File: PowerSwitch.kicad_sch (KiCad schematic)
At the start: 5 parts

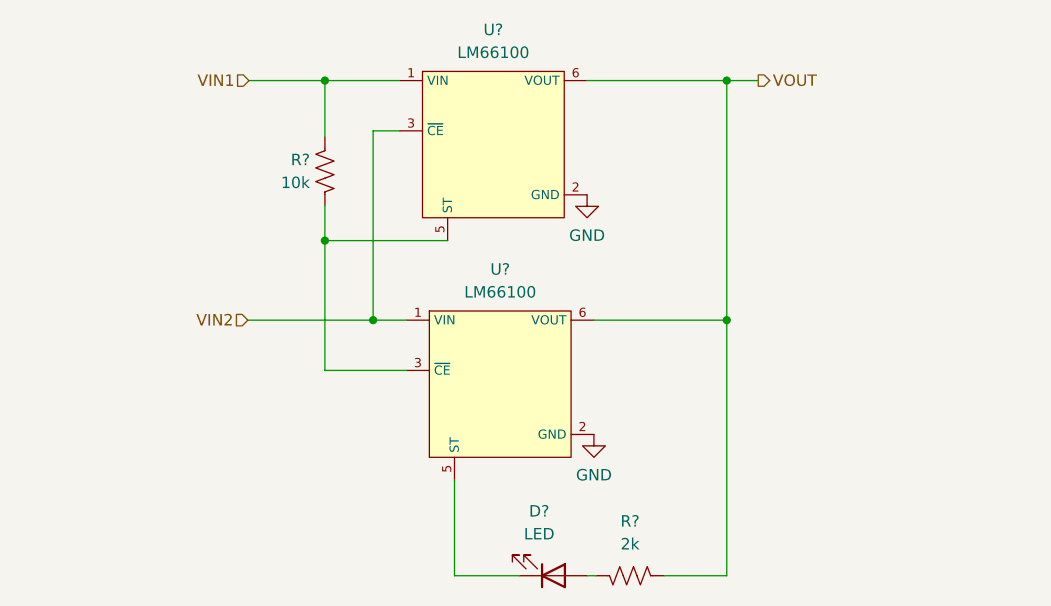
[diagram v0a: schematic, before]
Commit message: fixing sheet numbers and adding schematic PDF
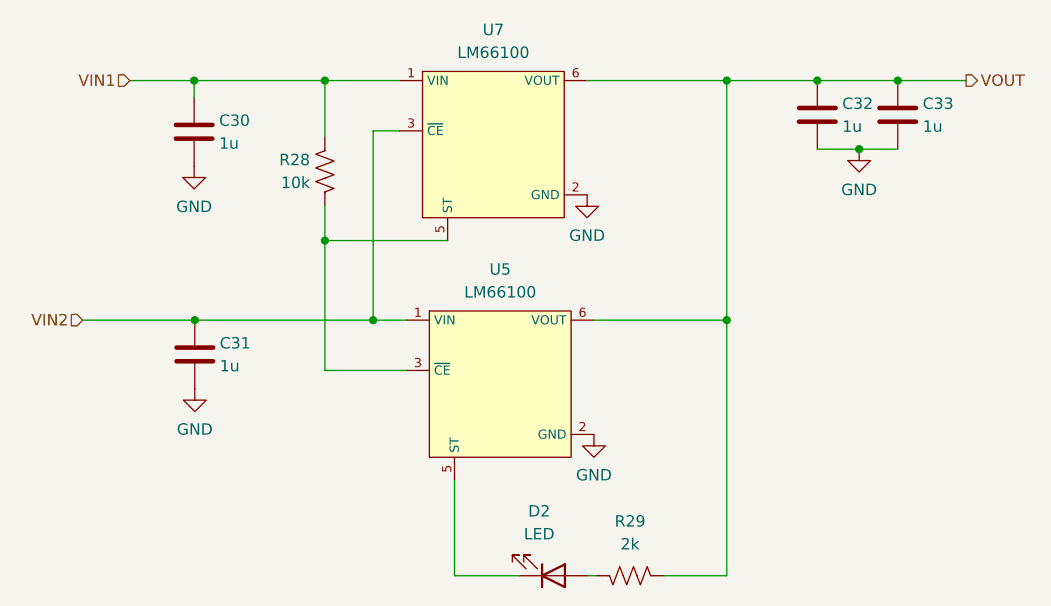
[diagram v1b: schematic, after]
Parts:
- added C30, C31, C32, C33: 1u, symbol Device:C
- gave numbers to parts that had none: 5
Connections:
- net GND: now also C30.2, C31.2, C32.2, C33.2
- net VIN1: now also C30.1
- net VIN2: now also C31.1
- net VOUT: now also C32.1, C33.1
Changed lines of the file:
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@@
   (junction (at 133.731 61.5188) (diameter 0) (color 0 0 0 0)
   )
+  (junction (at 119.2022 61.5188) (diameter 0) (color 0 0 0 0)
+  )
+  (junction (at 188.4426 61.5188) (diameter 0) (color 0 0 0 0)
+  )
   (junction (at 178.3842 88.138) (diameter 0) (color 0 0 0 0)
   )
@@
   (junction (at 133.731 79.2988) (diameter 0) (color 0 0 0 0)
   )
+  (junction (at 193.0908 69.1388) (diameter 0) (color 0 0 0 0)
+  )
+  (junction (at 119.2784 88.138) (diameter 0) (color 0 0 0 0)
+  )
+  (junction (at 197.3834 61.5188) (diameter 0) (color 0 0 0 0)
+  )
   (junction (at 178.3842 61.5188) (diameter 0) (color 0 0 0 0)
   )
+  (wire (pts (xy 119.2022 63.3984) (xy 119.2022 61.5188))
+    (stroke (width 0) (type default) (color 0 0 0 0))
+  )
   (wire (pts (xy 148.1328 116.5352) (xy 148.1328 105.918))
     (stroke (width 0) (type default) (color 0 0 0 0))
@@
     (stroke (width 0) (type default) (color 0 0 0 0))
   )
-  (wire (pts (xy 178.3842 61.5188) (xy 181.8894 61.5188))
+  (wire (pts (xy 178.3842 61.5188) (xy 188.4426 61.5188))
+    (stroke (width 0) (type default) (color 0 0 0 0))
+  )
+  (wire (pts (xy 119.2022 61.5188) (xy 133.731 61.5188))
     (stroke (width 0) (type default) (color 0 0 0 0))
   )
@@
     (stroke (width 0) (type default) (color 0 0 0 0))
   )
-  (wire (pts (xy 125.1712 88.138) (xy 139.0904 88.138))
+  (wire (pts (xy 106.8324 88.138) (xy 119.2784 88.138))
+    (stroke (width 0) (type default) (color 0 0 0 0))
+  )
+  (wire (pts (xy 119.2784 88.138) (xy 139.0904 88.138))
     (stroke (width 0) (type default) (color 0 0 0 0))
   )
@@
     (stroke (width 0) (type default) (color 0 0 0 0))
   )
+  (wire (pts (xy 188.4426 69.1388) (xy 193.0908 69.1388))
+    (stroke (width 0) (type default) (color 0 0 0 0))
+  )
   (wire (pts (xy 163.6268 88.138) (xy 178.3842 88.138))
     (stroke (width 0) (type default) (color 0 0 0 0))
   )
+  (wire (pts (xy 197.3834 61.5188) (xy 204.978 61.5188))
+    (stroke (width 0) (type default) (color 0 0 0 0))
+  )
   (wire (pts (xy 142.7988 93.726) (xy 133.731 93.726))
     (stroke (width 0) (type default) (color 0 0 0 0))
   )
-  (wire (pts (xy 125.2982 61.5188) (xy 133.731 61.5188))
+  (wire (pts (xy 188.4426 61.5188) (xy 197.3834 61.5188))
+    (stroke (width 0) (type default) (color 0 0 0 0))
+  )
+  (wire (pts (xy 112.0648 61.5188) (xy 119.2022 61.5188))
     (stroke (width 0) (type default) (color 0 0 0 0))
   )
@@
     (stroke (width 0) (type default) (color 0 0 0 0))
   )
-  (hierarchical_label "VIN1" (shape input) (at 125.2982 61.5188 180)
+  (wire (pts (xy 193.0908 69.1388) (xy 197.3834 69.1388))
+    (stroke (width 0) (type default) (color 0 0 0 0))
+  )
+  (hierarchical_label "VIN1" (shape input) (at 112.0648 61.5188 180)
     (effects (font (size 1.27 1.27)) (justify right))
   )
-  (hierarchical_label "VOUT" (shape output) (at 181.8894 61.5188 0)
+  (hierarchical_label "VOUT" (shape output) (at 204.978 61.5188 0)
     (effects (font (size 1.27 1.27)) (justify left))
   )
-  (hierarchical_label "VIN2" (shape input) (at 125.1712 88.138 180)
+  (hierarchical_label "VIN2" (shape input) (at 106.8324 88.138 180)
     (effects (font (size 1.27 1.27)) (justify right))
   )
   (symbol (lib_id "Device:R_US") (at 167.64 116.5352 270) (mirror x) (unit 1)
     (in_bom yes) (on_board yes) (fields_autoplaced)
-    (property "Reference" "R?" (id 0) (at 167.64 110.49 90))
+    (property "Reference" "R29" (id 0) (at 167.64 110.49 90))
     (property "Value" "2k" (id 1) (at 167.64 113.03 90))
     (property "Footprint" "" (id 2) (at 167.386 115.5192 90)
@@
     (pin "2")
   )
+  (symbol (lib_id "Device:C") (at 197.3834 65.3288 0) (unit 1)
+    (in_bom yes) (on_board yes)
+    (property "Reference" "C33" (id 0) (at 200.152 64.0842 0)
+      (effects (font (size 1.27 1.27)) (justify left))
+    )
+    (property "Value" "1u" (id 1) (at 200.152 66.6242 0)
+      (effects (font (size 1.27 1.27)) (justify left))
+    )
+    (property "Footprint" "" (id 2) (at 198.3486 69.1388 0)
+      (effects (font (size 1.27 1.27)) hide)
+    )
+    (property "Datasheet" "~" (id 3) (at 197.3834 65.3288 0)
+      (effects (font (size 1.27 1.27)) hide)
+    )
+    (pin "1")
+    (pin "2")
+  )
+  (symbol (lib_id "Device:C") (at 119.2022 67.2084 0) (unit 1)
+    (in_bom yes) (on_board yes)
+    (property "Reference" "C30" (id 0) (at 121.9708 65.9638 0)
+      (effects (font (size 1.27 1.27)) (justify left))
+    )
+    (property "Value" "1u" (id 1) (at 121.9708 68.5038 0)
+      (effects (font (size 1.27 1.27)) (justify left))
+    )
+    (property "Footprint" "" (id 2) (at 120.1674 71.0184 0)
+      (effects (font (size 1.27 1.27)) hide)
+    )
+    (property "Datasheet" "~" (id 3) (at 119.2022 67.2084 0)
+      (effects (font (size 1.27 1.27)) hide)
+    )
+    (pin "1")
+    (pin "2")
+  )
+  (symbol (lib_id "Device:C") (at 119.2784 91.948 0) (unit 1)
+    (in_bom yes) (on_board yes)
+    (property "Reference" "C31" (id 0) (at 122.047 90.7034 0)
+      (effects (font (size 1.27 1.27)) (justify left))
+    )
+    (property "Value" "1u" (id 1) (at 122.047 93.2434 0)
+      (effects (font (size 1.27 1.27)) (justify left))
+    )
+    (property "Footprint" "" (id 2) (at 120.2436 95.758 0)
+      (effects (font (size 1.27 1.27)) hide)
+    )
+    (property "Datasheet" "~" (id 3) (at 119.2784 91.948 0)
+      (effects (font (size 1.27 1.27)) hide)
+    )
+    (pin "1")
+    (pin "2")
+  )
+  (symbol (lib_id "power:GND") (at 119.2022 71.0184 0) (unit 1)
+    (in_bom yes) (on_board yes) (fields_autoplaced)
+    (property "Reference" "#PWR034" (id 0) (at 119.2022 77.3684 0)
+      (effects (font (size 1.27 1.27)) hide)
+    )
+    (property "Value" "GND" (id 1) (at 119.2022 75.5396 0))
+    (property "Footprint" "" (id 2) (at 119.2022 71.0184 0)
+      (effects (font (size 1.27 1.27)) hide)
+    )
+    (property "Datasheet" "" (id 3) (at 119.2022 71.0184 0)
+      (effects (font (size 1.27 1.27)) hide)
+    )
+    (pin "1")
+  )
+  (symbol (lib_id "power:GND") (at 193.0908 69.1388 0) (unit 1)
+    (in_bom yes) (on_board yes) (fields_autoplaced)
+    (property "Reference" "#PWR038" (id 0) (at 193.0908 75.4888 0)
+      (effects (font (size 1.27 1.27)) hide)
+    )
+    (property "Value" "GND" (id 1) (at 193.0908 73.66 0))
+    (property "Footprint" "" (id 2) (at 193.0908 69.1388 0)
+      (effects (font (size 1.27 1.27)) hide)
+    )
+    (property "Datasheet" "" (id 3) (at 193.0908 69.1388 0)
+      (effects (font (size 1.27 1.27)) hide)
+    )
+    (pin "1")
+  )
   (symbol (lib_id "Power_switch:LM66100") (at 153.4668 71.4248 0) (unit 1)
     (in_bom yes) (on_board yes) (fields_autoplaced)
-    (property "Reference" "U?" (id 0) (at 152.4508 55.88 0))
+    (property "Reference" "U7" (id 0) (at 152.4508 55.88 0))
     (property "Value" "LM66100" (id 1) (at 152.4508 58.42 0))
     (property "Footprint" "Package_TO_SOT_SMD:SOT-363_SC-70-6" (id 2) (at 153.4668 71.4248 0)
@@
   (symbol (lib_id "power:GND") (at 163.6268 100.838 0) (unit 1)
     (in_bom yes) (on_board yes) (fields_autoplaced)
-    (property "Reference" "#PWR?" (id 0) (at 163.6268 107.188 0)
+    (property "Reference" "#PWR037" (id 0) (at 163.6268 107.188 0)
       (effects (font (size 1.27 1.27)) hide)
     )
@@
   (symbol (lib_id "Device:LED") (at 159.131 116.5352 0) (mirror x) (unit 1)
     (in_bom yes) (on_board yes) (fields_autoplaced)
-    (property "Reference" "D?" (id 0) (at 157.5435 109.3724 0))
+    (property "Reference" "D2" (id 0) (at 157.5435 109.3724 0))
     (property "Value" "LED" (id 1) (at 157.5435 111.9124 0))
     (property "Footprint" "" (id 2) (at 159.131 116.5352 0)
@@
   (symbol (lib_id "Device:R_US") (at 133.731 71.6026 0) (mirror x) (unit 1)
     (in_bom yes) (on_board yes) (fields_autoplaced)
-    (property "Reference" "R?" (id 0) (at 132.08 70.3325 0)
+    (property "Reference" "R28" (id 0) (at 132.08 70.3325 0)
       (effects (font (size 1.27 1.27)) (justify right))
     )
@@
   (symbol (lib_id "Power_switch:LM66100") (at 154.2288 98.044 0) (unit 1)
     (in_bom yes) (on_board yes) (fields_autoplaced)
-    (property "Reference" "U?" (id 0) (at 153.2128 82.4992 0))
+    (property "Reference" "U5" (id 0) (at 153.2128 82.4992 0))
     (property "Value" "LM66100" (id 1) (at 153.2128 85.0392 0))
     (property "Footprint" "Package_TO_SOT_SMD:SOT-363_SC-70-6" (id 2) (at 154.2288 98.044 0)
@@
     (pin "6")
   )
+  (symbol (lib_id "power:GND") (at 119.2784 95.758 0) (unit 1)
+    (in_bom yes) (on_board yes) (fields_autoplaced)
+    (property "Reference" "#PWR035" (id 0) (at 119.2784 102.108 0)
+      (effects (font (size 1.27 1.27)) hide)
+    )
+    (property "Value" "GND" (id 1) (at 119.2784 100.2792 0))
+    (property "Footprint" "" (id 2) (at 119.2784 95.758 0)
+      (effects (font (size 1.27 1.27)) hide)
+    )
+    (property "Datasheet" "" (id 3) (at 119.2784 95.758 0)
+      (effects (font (size 1.27 1.27)) hide)
+    )
+    (pin "1")
+  )
   (symbol (lib_id "power:GND") (at 162.8648 74.2188 0) (unit 1)
     (in_bom yes) (on_board yes) (fields_autoplaced)
-    (property "Reference" "#PWR?" (id 0) (at 162.8648 80.5688 0)
+    (property "Reference" "#PWR068" (id 0) (at 162.8648 80.5688 0)
       (effects (font (size 1.27 1.27)) hide)
     )
@@
     (pin "1")
   )
+  (symbol (lib_id "Device:C") (at 188.4426 65.3288 0) (unit 1)
+    (in_bom yes) (on_board yes)
+    (property "Reference" "C32" (id 0) (at 191.2112 64.0842 0)
+      (effects (font (size 1.27 1.27)) (justify left))
+    )
+    (property "Value" "1u" (id 1) (at 191.2112 66.6242 0)
+      (effects (font (size 1.27 1.27)) (justify left))
+    )
+    (property "Footprint" "" (id 2) (at 189.4078 69.1388 0)
+      (effects (font (size 1.27 1.27)) hide)
+    )
+    (property "Datasheet" "~" (id 3) (at 188.4426 65.3288 0)
+      (effects (font (size 1.27 1.27)) hide)
+    )
+    (pin "1")
+    (pin "2")
+  )
 )

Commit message: Fixing ERC
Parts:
- renumbered C30 to C49, C31 to C50, C32 to C51, C33 to C52, R28 to R34, R29 to R35, U5 to U8
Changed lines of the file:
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@@
   (symbol (lib_id "Device:R_US") (at 167.64 116.5352 270) (mirror x) (unit 1)
     (in_bom yes) (on_board yes) (fields_autoplaced)
-    (property "Reference" "R29" (id 0) (at 167.64 110.49 90))
+    (property "Reference" "R35" (id 0) (at 167.64 110.49 90))
     (property "Value" "2k" (id 1) (at 167.64 113.03 90))
     (property "Footprint" "" (id 2) (at 167.386 115.5192 90)
@@
   (symbol (lib_id "Device:C") (at 197.3834 65.3288 0) (unit 1)
     (in_bom yes) (on_board yes)
-    (property "Reference" "C33" (id 0) (at 200.152 64.0842 0)
+    (property "Reference" "C52" (id 0) (at 200.152 64.0842 0)
       (effects (font (size 1.27 1.27)) (justify left))
     )
@@
   (symbol (lib_id "Device:C") (at 119.2022 67.2084 0) (unit 1)
     (in_bom yes) (on_board yes)
-    (property "Reference" "C30" (id 0) (at 121.9708 65.9638 0)
+    (property "Reference" "C49" (id 0) (at 121.9708 65.9638 0)
       (effects (font (size 1.27 1.27)) (justify left))
     )
@@
   (symbol (lib_id "Device:C") (at 119.2784 91.948 0) (unit 1)
     (in_bom yes) (on_board yes)
-    (property "Reference" "C31" (id 0) (at 122.047 90.7034 0)
+    (property "Reference" "C50" (id 0) (at 122.047 90.7034 0)
       (effects (font (size 1.27 1.27)) (justify left))
     )
@@
   (symbol (lib_id "power:GND") (at 119.2022 71.0184 0) (unit 1)
     (in_bom yes) (on_board yes) (fields_autoplaced)
-    (property "Reference" "#PWR034" (id 0) (at 119.2022 77.3684 0)
+    (property "Reference" "#PWR069" (id 0) (at 119.2022 77.3684 0)
       (effects (font (size 1.27 1.27)) hide)
     )
@@
   (symbol (lib_id "power:GND") (at 193.0908 69.1388 0) (unit 1)
     (in_bom yes) (on_board yes) (fields_autoplaced)
-    (property "Reference" "#PWR038" (id 0) (at 193.0908 75.4888 0)
+    (property "Reference" "#PWR073" (id 0) (at 193.0908 75.4888 0)
       (effects (font (size 1.27 1.27)) hide)
     )
@@
   (symbol (lib_id "power:GND") (at 163.6268 100.838 0) (unit 1)
     (in_bom yes) (on_board yes) (fields_autoplaced)
-    (property "Reference" "#PWR037" (id 0) (at 163.6268 107.188 0)
+    (property "Reference" "#PWR072" (id 0) (at 163.6268 107.188 0)
       (effects (font (size 1.27 1.27)) hide)
     )
@@
   (symbol (lib_id "Device:R_US") (at 133.731 71.6026 0) (mirror x) (unit 1)
     (in_bom yes) (on_board yes) (fields_autoplaced)
-    (property "Reference" "R28" (id 0) (at 132.08 70.3325 0)
+    (property "Reference" "R34" (id 0) (at 132.08 70.3325 0)
       (effects (font (size 1.27 1.27)) (justify right))
     )
@@
   (symbol (lib_id "Power_switch:LM66100") (at 154.2288 98.044 0) (unit 1)
     (in_bom yes) (on_board yes) (fields_autoplaced)
-    (property "Reference" "U5" (id 0) (at 153.2128 82.4992 0))
+    (property "Reference" "U8" (id 0) (at 153.2128 82.4992 0))
     (property "Value" "LM66100" (id 1) (at 153.2128 85.0392 0))
     (property "Footprint" "Package_TO_SOT_SMD:SOT-363_SC-70-6" (id 2) (at 154.2288 98.044 0)
@@
   (symbol (lib_id "power:GND") (at 119.2784 95.758 0) (unit 1)
     (in_bom yes) (on_board yes) (fields_autoplaced)
-    (property "Reference" "#PWR035" (id 0) (at 119.2784 102.108 0)
+    (property "Reference" "#PWR070" (id 0) (at 119.2784 102.108 0)
       (effects (font (size 1.27 1.27)) hide)
     )
@@
   (symbol (lib_id "power:GND") (at 162.8648 74.2188 0) (unit 1)
     (in_bom yes) (on_board yes) (fields_autoplaced)
-    (property "Reference" "#PWR068" (id 0) (at 162.8648 80.5688 0)
+    (property "Reference" "#PWR071" (id 0) (at 162.8648 80.5688 0)
       (effects (font (size 1.27 1.27)) hide)
     )
@@
   (symbol (lib_id "Device:C") (at 188.4426 65.3288 0) (unit 1)
     (in_bom yes) (on_board yes)
-    (property "Reference" "C32" (id 0) (at 191.2112 64.0842 0)
-      (effects (font (size 1.27 1.27)) (justify left))
-    )
+    (property "Reference" "C51" (id 0) (at 191.2112 64.0842 0)
+      (effects (font (size 1.27 1.27)) (justify left))
+    )
